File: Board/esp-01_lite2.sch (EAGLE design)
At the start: 17 parts, among them IC1 TINY13-20SU, K1 setup, K2 reset

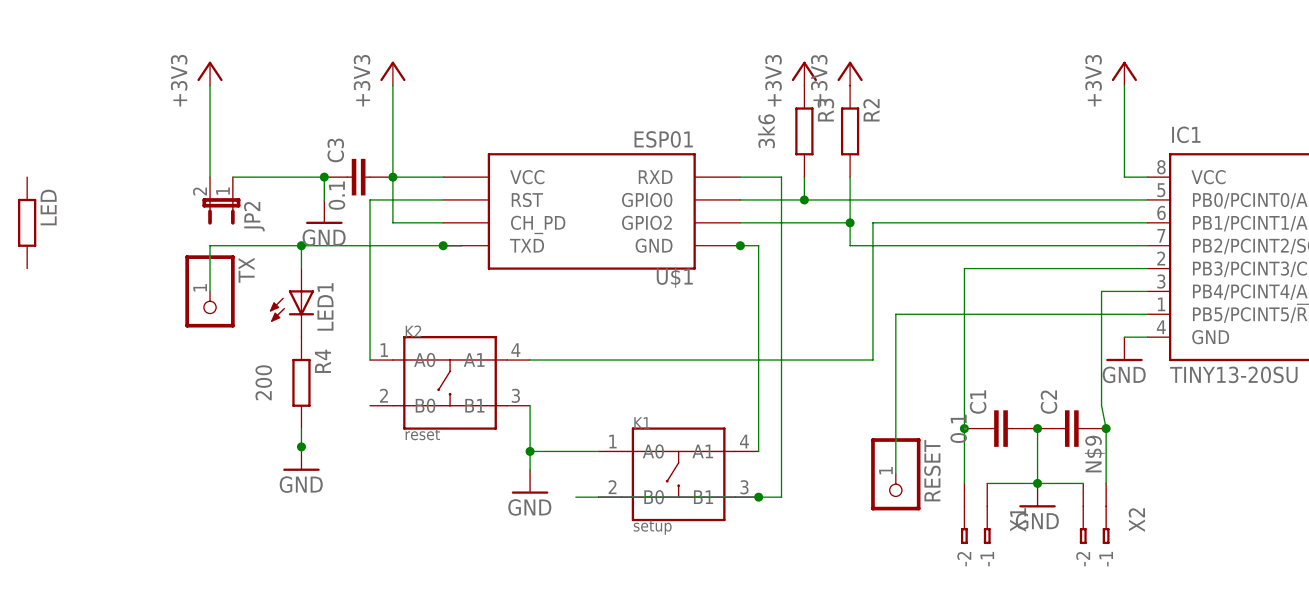
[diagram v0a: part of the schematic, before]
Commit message: add password
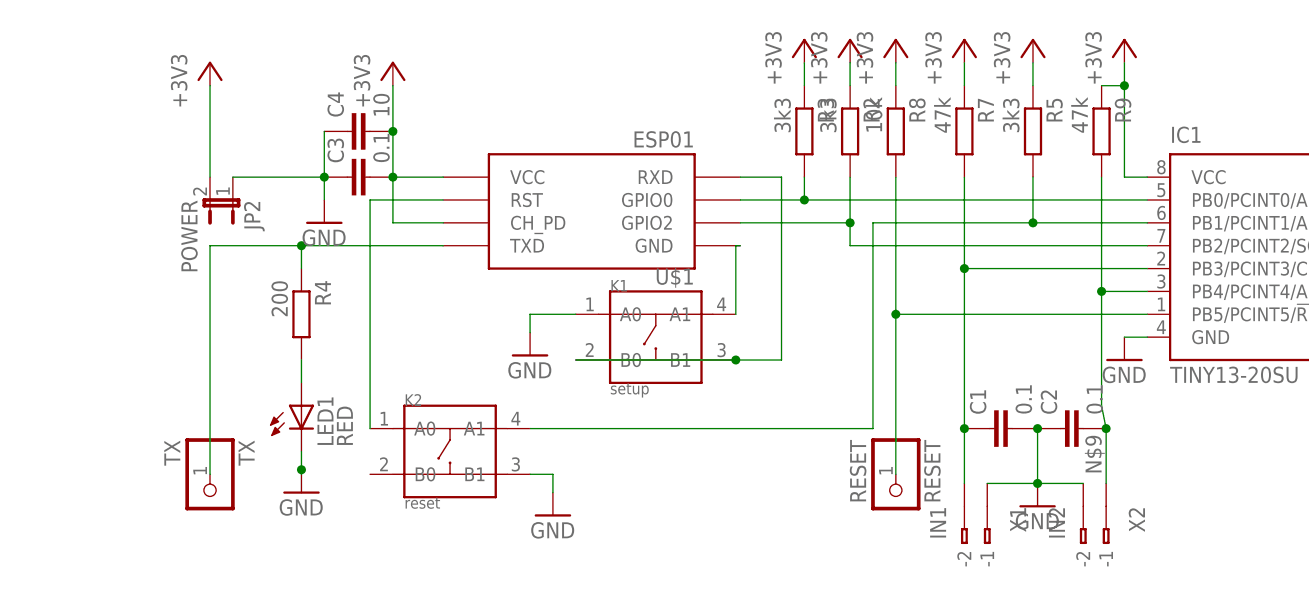
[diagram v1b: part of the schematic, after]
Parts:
- removed LED: (no value), resistor:R-EU_0207/5V
- added C4: 10, resistor:C-EU025-024X044
- added R5: 3k3, rcl:R-EU_R0805
- added R7: 47k, rcl:R-EU_R0805
- added R8: 10k, rcl:R-EU_R0805
- added R9: 47k, resistor:R-EU_0207/10
- C1, C2, C3: value (none) -> 0.1
- JP2: value (none) -> POWER
- LED1: value (none) -> RED; device led:LED3MM -> led:LEDSML0805
- R2, R3: value (none) -> 3k3
- R4: value (none) -> 200; device rcl:R-EU_R0805 -> resistor:R-EU_0207/5V
- RESET: value (none) -> RESET
- TX: value (none) -> TX
- X1: value (none) -> IN1
- X2: value (none) -> IN2
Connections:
- removed net N$1: LED1.C, R4.1
- new net N$12: LED1.A, R4.2
- net +3V3: now also C4.2, R5.1, R7.1, R8.1, R9.1
- net GND: now also C4.1, LED1.C; no longer R4.2
- net N$13: now also R8.2
- net N$15: now also R9.2
- net N$3: now also R4.1; no longer LED1.A
- net N$5: now also R5.2
- net N$9: now also R7.2
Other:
- moved on the sheet: K1, K2, LED1, R4, TX

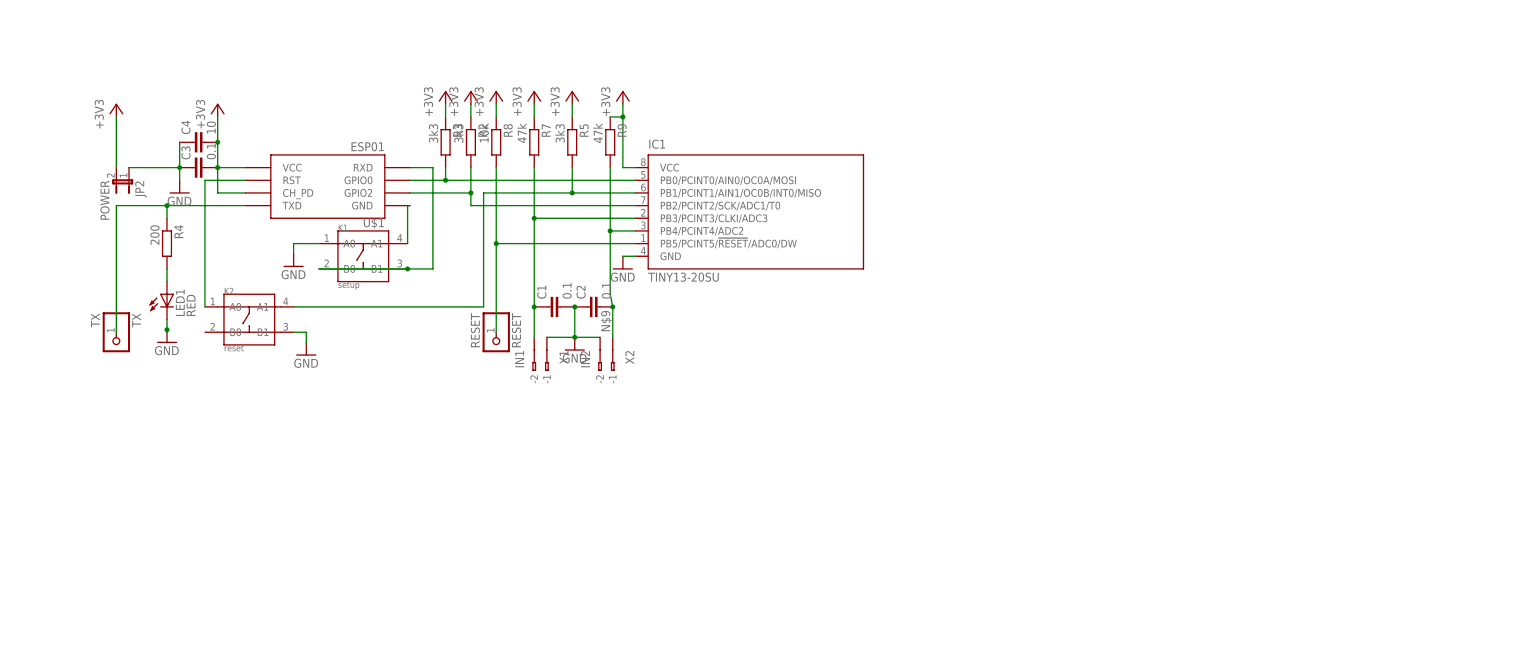
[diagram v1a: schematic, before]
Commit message: attiny84 250ms check
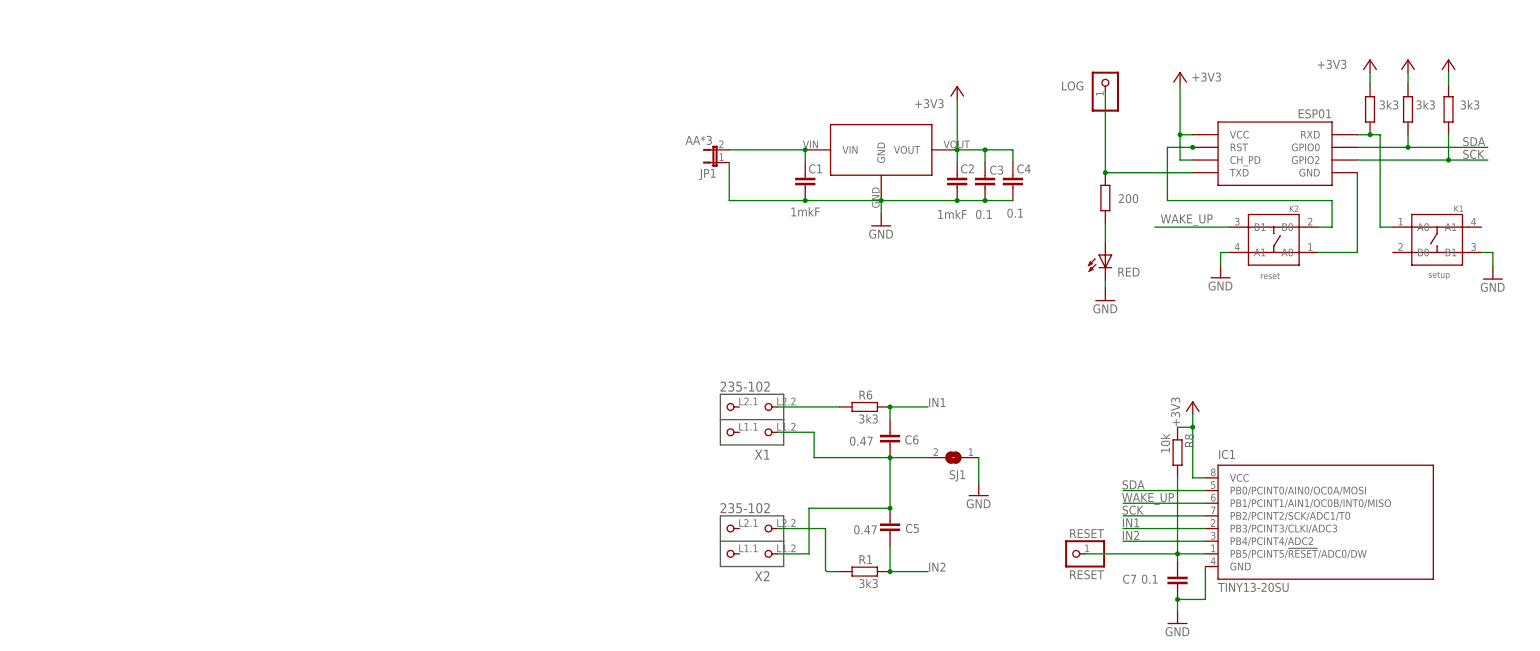
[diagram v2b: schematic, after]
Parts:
- removed JP2: POWER, jumper:JP1E
- removed R5: 3k3, rcl:R-EU_R0805
- removed R9: 47k, resistor:R-EU_0207/10
- removed TX: TX, pinhead:PINHD-1X1
- added C5, C6: 0.47, resistor:C-EUC0805
- added C7: 0.1, resistor:C-EUC0805
- added JP1: (no value), jumper:JP1E
- added LOG: LOG, pinhead:PINHD-1X1
- added R1, R6: 3k3, resistor:R-EU_M0805
- added SJ1: (no value), jumper:SJ
- added U$2: HT7333, HT7333_SOT89:HT7333
- C1, C2: value 0.1 -> 1mkF; device rcl:C-EUC0805 -> resistor:C-EUC0805; MKF 0.1 -> (none)
- C3: device rcl:C-EUC0805 -> resistor:C-EUC0805; MKF 0.1 -> (none)
- C4: value 10 -> 0.1; device resistor:C-EU025-024X044 -> resistor:C-EU050-024X044; MKF 0.1 -> (none)
- R7: value 47k -> 3k3
- X1: value IN1 -> 235-102; device con-wago:233-102 -> con-wago_235:235-102
- X2: value IN2 -> 235-102; device con-wago:233-102 -> con-wago_235:235-102; SPICEPREFIX (none) -> X
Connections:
- net N$2 renamed SDA
- net N$6 renamed SCK
- removed net N$10: K1.A1, U$1.GND
- removed net N$15: C2.2, IC1.PB4/PCINT4/ADC2, R9.2, X2.B-1
- removed net N$8: K2.A0, U$1.RST
- removed net N$9: C1.1, IC1.PB3/PCINT3/CLKI/ADC3, R7.2, X1.B-2
- new net AA*3: C1.2, JP1.2, U$2.VIN
- new net GND1: K2.A0, U$1.GND
- new net IN1: C6.2, IC1.PB3/PCINT3/CLKI/ADC3, R6.2
- new net IN2: C5.2, IC1.PB4/PCINT4/ADC2, R1.2
- new net LOG: LOG.1, R4.1, U$1.TXD
- new net N$2: K2.B0, U$1.RST
- new net RX: K1.A0, R7.2, U$1.RXD
- new net WAKE_UP: IC1.PB1/PCINT1/AIN1/OC0B/INT0/MISO, K2.B1
- net +3V3: now also C2.2, C4.1, U$2.VOUT; no longer C4.2, JP2.2, R5.1, R9.1
- net GND: now also C1.1, C4.2, C7.1, JP1.1, K1.B1, K2.A1, SJ1.1, U$2.GND; no longer C1.2, C4.1, JP2.1, K1.A0, K2.B1, X1.B-1, X2.B-2
- net N$13: now also C7.2
- net N$3: now also R6.1, X1.P2.2; no longer R4.1, TX.1, U$1.TXD
- net N$4: now also R1.1, X2.P2.2; no longer K1.B0, K1.B1, U$1.RXD
- net N$5: now also C5.1, C6.1, SJ1.2, X1.P1.2, X2.P1.2; no longer IC1.PB1/PCINT1/AIN1/OC0B/INT0/MISO, K2.A1, R5.2
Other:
- moved on the sheet: C1, C2, C3, C4, IC1, K1, K2, R8, RESET

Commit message: LED works, server ok, ESP 24h
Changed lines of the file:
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@@
 <grid distance="10" unitdist="mil" unit="mil" style="lines" multiple="1" display="no" altdistance="0.01" altunitdist="inch" altunit="inch"/>
 <layers>
-<layer number="1" name="Top" color="4" fill="1" visible="no" active="no"/>
-<layer number="2" name="Route2" color="1" fill="3" visible="no" active="no"/>
-<layer number="3" name="Route3" color="4" fill="3" visible="no" active="no"/>
-<layer number="4" name="Route4" color="1" fill="4" visible="no" active="no"/>
-<layer number="5" name="Route5" color="4" fill="4" visible="no" active="no"/>
-<layer number="6" name="Route6" color="1" fill="8" visible="no" active="no"/>
-<layer number="7" name="Route7" color="4" fill="8" visible="no" active="no"/>
-<layer number="8" name="Route8" color="1" fill="2" visible="no" active="no"/>
-<layer number="9" name="Route9" color="4" fill="2" visible="no" active="no"/>
-<layer number="10" name="Route10" color="1" fill="7" visible="no" active="no"/>
-<layer number="11" name="Route11" color="4" fill="7" visible="no" active="no"/>
-<layer number="12" name="Route12" color="1" fill="5" visible="no" active="no"/>
-<layer number="13" name="Route13" color="4" fill="5" visible="no" active="no"/>
-<layer number="14" name="Route14" color="1" fill="6" visible="no" active="no"/>
-<layer number="15" name="Route15" color="4" fill="6" visible="no" active="no"/>
-<layer number="16" name="Bottom" color="1" fill="1" visible="no" active="no"/>
-<layer number="17" name="Pads" color="2" fill="1" visible="no" active="no"/>
-<layer number="18" name="Vias" color="2" fill="1" visible="no" active="no"/>
-<layer number="19" name="Unrouted" color="6" fill="1" visible="no" active="no"/>
-<layer number="20" name="Dimension" color="15" fill="1" visible="no" active="no"/>
-<layer number="21" name="tPlace" color="7" fill="1" visible="no" active="no"/>
-<layer number="22" name="bPlace" color="7" fill="1" visible="no" active="no"/>
-<layer number="23" name="tOrigins" color="15" fill="1" visible="no" active="no"/>
-<layer number="24" name="bOrigins" color="15" fill="1" visible="no" active="no"/>
-<layer number="25" name="tNames" color="7" fill="1" visible="no" active="no"/>
-<layer number="26" name="bNames" color="7" fill="1" visible="no" active="no"/>
-<layer number="27" name="tValues" color="7" fill="1" visible="no" active="no"/>
-<layer number="28" name="bValues" color="7" fill="1" visible="no" active="no"/>
+<layer number="1" name="Top" color="4" fill="1" visible="yes" active="no"/>
+<layer number="2" name="Route2" color="1" fill="3" visible="yes" active="no"/>
+<layer number="3" name="Route3" color="4" fill="3" visible="yes" active="no"/>
+<layer number="4" name="Route4" color="1" fill="4" visible="yes" active="no"/>
+<layer number="5" name="Route5" color="4" fill="4" visible="yes" active="no"/>
+<layer number="6" name="Route6" color="1" fill="8" visible="yes" active="no"/>
+<layer number="7" name="Route7" color="4" fill="8" visible="yes" active="no"/>
+<layer number="8" name="Route8" color="1" fill="2" visible="yes" active="no"/>
+<layer number="9" name="Route9" color="4" fill="2" visible="yes" active="no"/>
+<layer number="10" name="Route10" color="1" fill="7" visible="yes" active="no"/>
+<layer number="11" name="Route11" color="4" fill="7" visible="yes" active="no"/>
+<layer number="12" name="Route12" color="1" fill="5" visible="yes" active="no"/>
+<layer number="13" name="Route13" color="4" fill="5" visible="yes" active="no"/>
+<layer number="14" name="Route14" color="1" fill="6" visible="yes" active="no"/>
+<layer number="15" name="Route15" color="4" fill="6" visible="yes" active="no"/>
+<layer number="16" name="Bottom" color="1" fill="1" visible="yes" active="no"/>
+<layer number="17" name="Pads" color="2" fill="1" visible="yes" active="no"/>
+<layer number="18" name="Vias" color="2" fill="1" visible="yes" active="no"/>
+<layer number="19" name="Unrouted" color="6" fill="1" visible="yes" active="no"/>
+<layer number="20" name="Dimension" color="15" fill="1" visible="yes" active="no"/>
+<layer number="21" name="tPlace" color="7" fill="1" visible="yes" active="no"/>
+<layer number="22" name="bPlace" color="7" fill="1" visible="yes" active="no"/>
+<layer number="23" name="tOrigins" color="15" fill="1" visible="yes" active="no"/>
+<layer number="24" name="bOrigins" color="15" fill="1" visible="yes" active="no"/>
+<layer number="25" name="tNames" color="7" fill="1" visible="yes" active="no"/>
+<layer number="26" name="bNames" color="7" fill="1" visible="yes" active="no"/>
+<layer number="27" name="tValues" color="7" fill="1" visible="yes" active="no"/>
+<layer number="28" name="bValues" color="7" fill="1" visible="yes" active="no"/>
 <layer number="29" name="tStop" color="7" fill="3" visible="no" active="no"/>
 <layer number="30" name="bStop" color="7" fill="6" visible="no" active="no"/>
@@
 <layer number="35" name="tGlue" color="7" fill="4" visible="no" active="no"/>
 <layer number="36" name="bGlue" color="7" fill="5" visible="no" active="no"/>
-<layer number="37" name="tTest" color="7" fill="1" visible="no" active="no"/>
-<layer number="38" name="bTest" color="7" fill="1" visible="no" active="no"/>
+<layer number="37" name="tTest" color="7" fill="1" visible="yes" active="no"/>
+<layer number="38" name="bTest" color="7" fill="1" visible="yes" active="no"/>
 <layer number="39" name="tKeepout" color="4" fill="11" visible="no" active="no"/>
 <layer number="40" name="bKeepout" color="1" fill="11" visible="no" active="no"/>
@@
 <layer number="44" name="Drills" color="7" fill="1" visible="no" active="no"/>
 <layer number="45" name="Holes" color="7" fill="1" visible="no" active="no"/>
-<layer number="46" name="Milling" color="3" fill="1" visible="no" active="no"/>
-<layer number="47" name="Measures" color="7" fill="1" visible="no" active="no"/>
-<layer number="48" name="Document" color="7" fill="1" visible="no" active="no"/>
-<layer number="49" name="Reference" color="7" fill="1" visible="no" active="no"/>
-<layer number="50" name="dxf" color="7" fill="1" visible="no" active="no"/>
-<layer number="51" name="tDocu" color="7" fill="1" visible="no" active="no"/>
-<layer number="52" name="bDocu" color="7" fill="1" visible="no" active="no"/>
-<layer number="53" name="tGND_GNDA" color="7" fill="9" visible="no" active="no"/>
-<layer number="54" name="bGND_GNDA" color="1" fill="9" visible="no" active="no"/>
-<layer number="56" name="wert" color="7" fill="1" visible="no" active="no"/>
-<layer number="57" name="tCAD" color="7" fill="1" visible="no" active="no"/>
+<layer number="46" name="Milling" color="3" fill="1" visible="yes" active="no"/>
+<layer number="47" name="Measures" color="7" fill="1" visible="yes" active="no"/>
+<layer number="48" name="Document" color="7" fill="1" visible="yes" active="no"/>
+<layer number="49" name="Reference" color="7" fill="1" visible="yes" active="no"/>
+<layer number="50" name="dxf" color="7" fill="1" visible="yes" active="no"/>
+<layer number="51" name="tDocu" color="7" fill="1" visible="yes" active="no"/>
+<layer number="52" name="bDocu" color="7" fill="1" visible="yes" active="no"/>
+<layer number="53" name="tGND_GNDA" color="7" fill="9" visible="yes" active="no"/>
+<layer number="54" name="bGND_GNDA" color="1" fill="9" visible="yes" active="no"/>
+<layer number="56" name="wert" color="7" fill="1" visible="yes" active="no"/>
+<layer number="57" name="tCAD" color="7" fill="1" visible="yes" active="no"/>
 <layer number="90" name="Modules" color="5" fill="1" visible="yes" active="yes"/>
 <layer number="91" name="Nets" color="2" fill="1" visible="yes" active="yes"/>
@@
 <attribute name="VALUE" x="140.208" y="110.49" size="1.778" layer="96" rot="R180"/>
 </instance>
-<instance part="SJ1" gate="1" x="61.214" y="30.734" rot="R180"/>
+<instance part="SJ1" gate="1" x="61.214" y="30.734" smashed="yes" rot="R180">
+<attribute name="NAME" x="63.754" y="28.194" size="1.778" layer="95" rot="R180"/>
+<attribute name="VALUE" x="63.754" y="34.544" size="1.778" layer="96" rot="R180"/>
+</instance>
 <instance part="GND4" gate="1" x="66.294" y="23.114" smashed="yes">
 <attribute name="VALUE" x="63.754" y="20.574" size="1.778" layer="96"/>

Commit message: new board
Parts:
- added C8: 0.1, resistor:C-EUC0805
- added R5: 10k, rcl:R-EU_R0805
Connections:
- removed net LOG: LOG.1, R4.1, U$1.TXD
- removed net N$12: LED1.A, R4.2
- new net N$1: LED1.A, LOG.1, U$1.TXD
- new net N$6: LED1.C, R4.1
- net +3V3: now also R5.1
- net GND: now also C8.1, K1.B0, R4.2; no longer LED1.C
- net N$2: now also R5.2
- net RX: now also K1.A1; no longer K1.A0
- net WAKE_UP: now also C8.2
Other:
- moved on the sheet: K1

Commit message: board for one_button
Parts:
- removed C3, C8: 0.1, resistor:C-EUC0805
- removed K1: setup, Seeed-OPL-Button:DIP-BUTTON-4P
- removed K2: reset, Seeed-OPL-Button:DIP-BUTTON-4P
- removed RESET: RESET, pinhead:PINHD-1X1
- removed SJ1: (no value), jumper:SJ
- removed X1, X2: 235-102, con-wago_235:235-102
- added C9: 10mkF, rcl:C-EU025-030X050
- added R10: 3k3, resistor:R-EU_M0805
- added R11: 200, rcl:R-EU_R0805
- added RST: RST, pinhead:PINHD-1X1
- added S2: (no value), switch-omron:31-XX
- added X3: (no value), con-wago255:233-104
- C4: device resistor:C-EU050-024X044 -> rcl:C-EUC0805
- R3: device resistor:R-EU_0207/5V -> rcl:R-EU_R0805
- R4: device resistor:R-EU_0207/5V -> rcl:R-EU_0207/2V
- R5: value 10k -> 3k3
- R8: value 10k -> 3k3; device rcl:R-EU_R0805 -> rcl:R-EU_0204/5
- U$2: value HT7333 -> MCP1700T-3302E/TT; device HT7333_SOT89:HT7333 -> MCP1700T-3302E_TT:MCP1700T-3302E/TT
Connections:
- removed net N$5: C5.1, C6.1, SJ1.2, X1.P1.2, X2.P1.2
- new net N$11: R5.2, U$1.RST
- net +3V3: now also C2.1, U$2.2; no longer C2.2, C3.2, U$1.CH_PD, U$2.VOUT
- net AA*3: now also C1.1, C9.1, U$2.3; no longer C1.2, U$2.VIN
- net GND: now also C1.2, C2.2, C9.2, R10.2, U$1.GND, U$2.1; no longer C1.1, C2.1, C3.1, C8.1, K1.B0, K1.B1, K2.A1, SJ1.1, U$2.GND
- net GND1: now also C5.1, C6.1, R10.1, R11.2, X3.-2, X3.-4; no longer K2.A0, U$1.GND
- net IN1: now also C5.2, R1.2; no longer C6.2, R6.2
- net IN2: now also C6.2, R6.2; no longer C5.2, R1.2
- net N$13: now also RST.1; no longer RESET.1
- net N$2: now also R11.1, S2.P; no longer K2.B0, R5.2, U$1.RST
- net N$3: now also X3.-1; no longer X1.P2.2
- net N$4: now also X3.-3; no longer X2.P2.2
- net RX: no longer K1.A1
- net SCK: now also S2.S
- net WAKE_UP: now also U$1.CH_PD; no longer C8.2, K2.B1
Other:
- moved on the sheet: C1, C2, C4, C5, C6, C7, IC1, JP1, R1, R5, R6, R8
